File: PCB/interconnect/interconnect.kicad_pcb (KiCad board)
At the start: 2 copper layers, 85 x 56.9 mm, 31 parts, among them J201 XT60-M, J202 5.08mm Screw Terminal, J203 Conn_01x03, J204 Conn_01x03, J205 Conn_01x03, J206 Conn_01x04, J301 Conn_01x15, J302 Conn_01x15, J501 Conn_01x04, J601 Conn_01x04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

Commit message: PCB Rev 1
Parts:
- moved C203 75.0 mm to (136.3, 83.1), turned to 0 degrees
- moved J205 67.8 mm to (132.6, 86.2), turned to 90 degrees
- moved C302 6.22 mm to (109.7, 123.4)
- moved C202 5.08 mm to (63.0, 91.9)
- moved J204 5.08 mm to (67.2, 95.1)
- moved D201 4.08 mm to (127.5, 119.2)
- moved R401 3.95 mm to (68.8, 112.9)
- moved Q401 3.86 mm to (65.6, 110.6)
- moved C201 3.86 mm to (65.6, 113.8)
- moved J203 2.54 mm to (67.2, 116.7)
- moved J201 1.65 mm to (132.0, 108.5)
- moved J202 1.54 mm to (134.8, 123.7)
- moved J701 1.27 mm to (74.2, 116.7)
- moved C701 1.27 mm to (75.5, 119.9)
- moved J206 1.13 mm to (119.9, 104.0)
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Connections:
- J301 pad 10: /MCUs/ESP32_D27 -> /Connectors/MOTORS.Steering
- J301 pad 11: /MCUs/ESP32_D14 -> /Connectors/MOTORS.ESC
- J301 pad 12: /Connectors/ULTRASONICS.US1_TRIGG -> /Connectors/ULTRASONICS.US1_ECHO
- J301 pad 13: /Connectors/ULTRASONICS.US1_ECHO -> /Connectors/ULTRASONICS.US1_TRIGG
- J301 pad 6: /Connectors/ULTRASONICS.US3_TRIGG -> /Connectors/ULTRASONICS.US3_ECHO
- J301 pad 7: /Connectors/ULTRASONICS.US3_ECHO -> /Connectors/ULTRASONICS.US3_TRIGG
- J301 pad 8: /Connectors/ULTRASONICS.US2_TRIGG -> /Connectors/ULTRASONICS.US2_ECHO
- J301 pad 9: /Connectors/ULTRASONICS.US2_ECHO -> /Connectors/ULTRASONICS.US2_TRIGG
- J302 pad 1: /MCUs/ESP32_D23 -> /Connectors/MOTORS.Magnet
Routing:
- net +5V: track 0.00 -> 158.4 mm, vias 0 -> 4
- net +3V3: track 0.00 -> 40.4 mm
- net /Connectors/MOTORS.Steering: track 0.00 -> 33.1 mm
- net /Connectors/MOTORS.Magnet: track 0.00 -> 24.9 mm
- net /Connectors/MOTORS.ESC: track 0.00 -> 21.9 mm
- net /Connectors/ULTRASONICS.US3_TRIGG: track 0.00 -> 15.0 mm
- net /Connectors/XIAO.SCL: track 0.00 -> 14.5 mm
- net /Connectors/ULTRASONICS.US2_TRIGG: track 0.00 -> 12.4 mm
- net /Connectors/ULTRASONICS.US1_TRIGG: track 0.00 -> 11.8 mm
- net /Connectors/ULTRASONICS.US3_ECHO: track 0.00 -> 11.6 mm
- net /Connectors/XIAO.SDA: track 0.00 -> 10.9 mm
- net /Connectors/ULTRASONICS.US1_ECHO: track 0.00 -> 10.6 mm
- net /Connectors/ULTRASONICS.US2_ECHO: track 0.00 -> 9.31 mm
- net /MCUs/ESP32_D15: track 0.00 -> 7.28 mm
- net Net-(Q401-G): track 0.00 -> 2.40 mm
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- added copper zone on F.Cu, net +3V3
- added copper zone on F.Cu, net +5V
- added copper zone on F.Cu, net /Connectors/ESC_5V
- added copper zone on F.Cu, net /Connectors/Magnet_+
- added copper zone on F.Cu, net /Connectors/Motor_Batt_+
- added copper zone on B.Cu, net GND
- added copper zone on F.Cu, net GND
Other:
- board text added: "C"
- board text added: "CAM"
- board text added: "D"

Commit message: Order
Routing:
- net GND: vias 58 -> 60
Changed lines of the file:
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@@
 		(sheetname "Ultrasonic3")
 		(sheetfile "Ultrasonic.kicad_sch")
-		(attr through_hole)
+		(attr through_hole dnp)
 		(fp_line
 			(start -1.33 -1.33)
@@
 		)
 		(fp_text user "${REFERENCE}"
-			(at 0 3.81 360)
+			(at 0 3.81 0)
 			(layer "F.Fab")
 			(effects
@@
 		(sheetname "Connectors")
 		(sheetfile "connectors.kicad_sch")
-		(attr through_hole)
+		(attr through_hole dnp)
 		(fp_line
 			(start -1.33 6.41)
@@
 		(tags "capacitor")
 		(property "Reference" "C601"
-			(at 0 -1.68 360)
+			(at 0 -1.68 0)
 			(layer "F.SilkS")
 			(hide yes)
@@
 		)
 		(property "Value" "1uF"
-			(at 0 1.68 360)
+			(at 0 1.68 0)
 			(layer "F.Fab")
 			(effects
@@
 		)
 		(fp_text user "${REFERENCE}"
-			(at 0 0 360)
+			(at 0 0 0)
 			(layer "F.Fab")
 			(effects
@@
 		(sheetname "Connectors")
 		(sheetfile "connectors.kicad_sch")
-		(attr through_hole)
+		(attr through_hole dnp)
 		(fp_line
 			(start 1.33 1.27)
@@
 		(sheetname "Connectors")
 		(sheetfile "connectors.kicad_sch")
-		(attr through_hole)
+		(attr through_hole dnp)
 		(fp_line
 			(start -1.33 -1.33)
@@
 		)
 		(fp_text user "${REFERENCE}"
-			(at 0 2.54 360)
+			(at 0 2.54 0)
 			(layer "F.Fab")
 			(effects
@@
 		(sheetname "Connectors")
 		(sheetfile "connectors.kicad_sch")
-		(attr through_hole)
+		(attr through_hole dnp)
 		(fp_line
 			(start 7.68 -5.261)
@@
 		(sheetname "MCUs")
 		(sheetfile "MCUs.kicad_sch")
-		(attr through_hole)
+		(attr through_hole dnp)
 		(fp_line
 			(start -1.33 -1.33)
@@
 		(sheetname "Ultrasonic1")
 		(sheetfile "Ultrasonic.kicad_sch")
-		(attr through_hole)
+		(attr through_hole dnp)
 		(fp_line
 			(start -1.33 -1.33)
@@
 		)
 		(fp_text user "${REFERENCE}"
-			(at 0 3.81 360)
+			(at 0 3.81 0)
 			(layer "F.Fab")
 			(effects
@@
 		(sheetname "Ultrasonic2")
 		(sheetfile "Ultrasonic.kicad_sch")
-		(attr through_hole)
+		(attr through_hole dnp)
 		(fp_line
 			(start -1.33 -1.33)
@@
 		)
 		(fp_text user "${REFERENCE}"
-			(at 0 3.81 360)
+			(at 0 3.81 0)
 			(layer "F.Fab")
 			(effects
@@
 		(tags "capacitor")
 		(property "Reference" "C701"
-			(at 0 -1.68 360)
+			(at 0 -1.68 0)
 			(layer "F.SilkS")
 			(hide yes)
@@
 		)
 		(property "Value" "1uF"
-			(at 0 1.68 360)
+			(at 0 1.68 0)
 			(layer "F.Fab")
 			(effects
@@
 		)
 		(fp_text user "${REFERENCE}"
-			(at 0 0 360)
+			(at 0 0 0)
 			(layer "F.Fab")
 			(effects
@@
 		(tags "capacitor")
 		(property "Reference" "C501"
-			(at 0 -1.68 360)
+			(at 0 -1.68 0)
 			(layer "F.SilkS")
 			(hide yes)
@@
 		)
 		(property "Value" "1uF"
-			(at 0 1.68 360)
+			(at 0 1.68 0)
 			(layer "F.Fab")
 			(effects
@@
 		)
 		(fp_text user "${REFERENCE}"
-			(at 0 0 360)
+			(at 0 0 0)
 			(layer "F.Fab")
 			(effects
@@
 		(sheetname "Connectors")
 		(sheetfile "connectors.kicad_sch")
-		(attr through_hole)
+		(attr through_hole dnp)
 		(fp_line
 			(start -9.5 0)
@@
 		(tags "capacitor")
 		(property "Reference" "C203"
-			(at 0 -1.68 360)
+			(at 0 -1.68 0)
 			(layer "F.SilkS")
 			(hide yes)
@@
 		)
 		(property "Value" "1uF"
-			(at 0 1.68 360)
+			(at 0 1.68 0)
 			(layer "F.Fab")
 			(effects
@@
 		)
 		(fp_text user "${REFERENCE}"
-			(at 0 0 360)
+			(at 0 0 0)
 			(layer "F.Fab")
 			(effects
@@
 		(sheetname "Connectors")
 		(sheetfile "connectors.kicad_sch")
-		(attr through_hole)
+		(attr through_hole dnp)
 		(fp_line
 			(start -1.33 6.41)
@@
 		(sheetname "MCUs")
 		(sheetfile "MCUs.kicad_sch")
-		(attr through_hole)
+		(attr through_hole dnp)
 		(fp_line
 			(start -1.33 -1.33)
@@
 	)
 	(gr_text "P"
-		(at 69.73 119.25 0)
+		(at 69.83 116.79 0)
 		(layer "F.SilkS")
 		(effects
@@
 		)
 	)
+	(gr_text "+"
+		(at 125.73 120.69 0)
+		(layer "F.SilkS")
+		(effects
+			(font
+				(size 1.27 1.27)
+				(thickness 0.1)
+			)
+		)
+	)
+	(gr_text "-"
+		(at 125.73 117.79 0)
+		(layer "F.SilkS")
+		(effects
+			(font
+				(size 1.27 1.27)
+				(thickness 0.1)
+			)
+		)
+	)
 	(segment
 		(start 74.505 117.03)
@@
 	)
 	(via
+		(at 72.93 114.69)
+		(size 0.35)
+		(drill 0.2)
+		(layers "F.Cu" "B.Cu")
+		(free yes)
+		(net 2)
+	)
+	(via
 		(at 89.95 110.89)
 		(size 0.35)
@@
 		(size 0.35)
 		(drill 0.2)
+		(layers "F.Cu" "B.Cu")
+		(free yes)
+		(net 2)
+	)
+	(via
+		(at 75.53 114.59)
+		(size 0.35)
+		(drill 0.2)

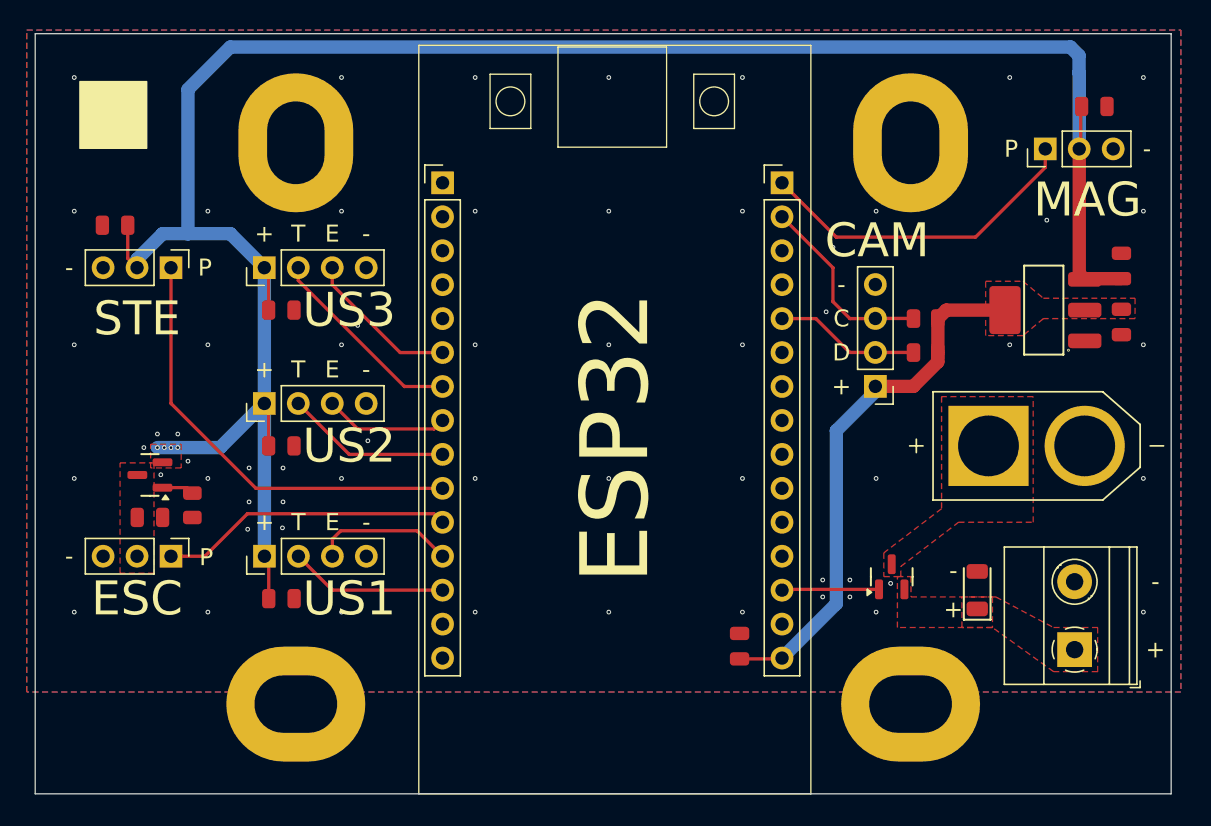
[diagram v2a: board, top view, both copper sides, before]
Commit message: Updated PCB, working inference
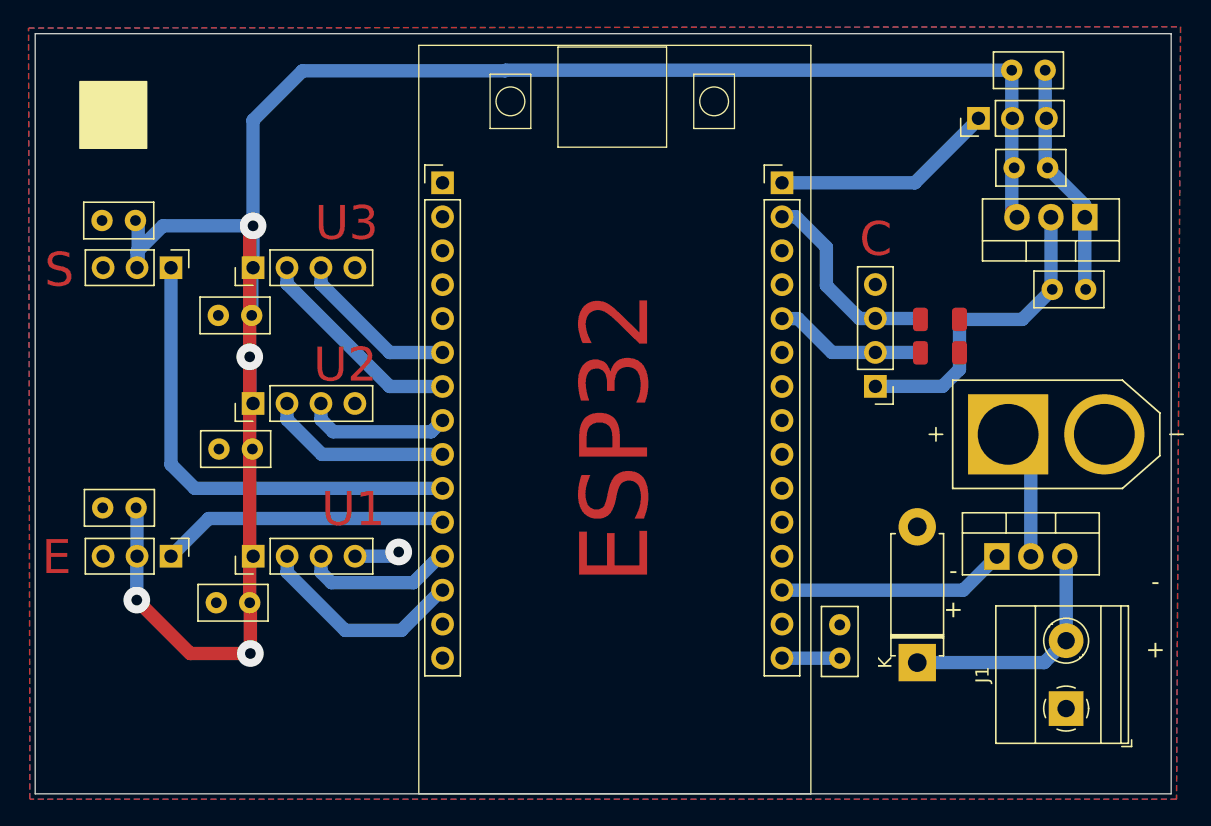
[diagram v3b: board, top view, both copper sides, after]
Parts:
- removed H201, H202, H203, H204: MountingHole_Pad, MountingHole:MountingHole_4.3x6.2mm_M4_Pad
- removed J202: 5.08mm Screw Terminal, TerminalBlock_Phoenix:TerminalBlock_Phoenix_MKDS-1,5-2-5.08_1x02_P5.08mm_Horizontal
- removed Q201: AO3400A, PCM_JLCPCB:Q_SOT-23
- removed Q401: AO3401A, PCM_JLCPCB:Q_SOT-23
- removed R401: 10kΩ, PCM_JLCPCB:R_0805
- removed U401: AMS1117, PCM_JLCPCB:SOT-223-3_L6.5-W3.4-P2.30-LS7.0-BR
- added J1: 5.08mm Screw Terminal, TerminalBlock_Phoenix:TerminalBlock_Phoenix_MKDS-1,5-2-5.08_1x02_P5.08mm_Horizontal, F.Cu at (134.2, 128.1)
- added Q1: IPP060N06N, Package_TO_SOT_THT:TO-220-3_Vertical, F.Cu at (129.0, 116.7)
- added U1: LM317_TO-220, Package_TO_SOT_THT:TO-220-3_Vertical, F.Cu at (135.6, 91.3)
- C201, C202, C203, C302, C401, C402, C501, C601, C701: footprint PCM_JLCPCB:C_0805 -> Capacitor_THT:C_Disc_D5.0mm_W2.5mm_P2.50mm
- D201: footprint PCM_JLCPCB:D_SOD-123FL -> Diode_THT:D_5W_P10.16mm_Horizontal
- R301, R302: footprint PCM_JLCPCB:R_0805 -> PCM_JLCPCB:R_1206
- moved C402 10.9 mm to (130.3, 87.6), turned to 0 degrees
- moved C302 7.55 mm to (117.2, 124.3)
- moved D201 7.04 mm to (123.0, 124.7)
- moved C203 6.75 mm to (130.1, 80.3)
- moved C401 5.73 mm to (133.1, 96.7), turned to 0 degrees
- moved J205 5.50 mm to (127.6, 83.9)
- moved C701 2.39 mm to (73.1, 120.2), turned to 180 degrees
- moved C501 2.25 mm to (73.2, 98.7), turned to 180 degrees
- moved C601 2.18 mm to (73.3, 108.7), turned to 180 degrees
- moved J201 1.71 mm to (133.4, 107.6)
- moved C202 1.57 mm to (64.5, 91.6)
- moved C201 1.26 mm to (64.6, 113.1), turned to 180 degrees
- moved R301 1.07 mm to (124.7, 99.0)
- moved R302 1.07 mm to (124.7, 101.5)
- moved J501 0.84 mm to (73.3, 95.1)
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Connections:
- C201 pad 1: /Connectors/ESC_5V -> +5V
- J203 pad 2: /Connectors/ESC_5V -> +5V
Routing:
- net GND: track 0.00 -> 21.1 mm, vias 60 -> 1
- net /Connectors/Magnet_+: track 0.00 -> 18.2 mm
- net +3V3: track 40.4 -> 28.2 mm
- net /MCUs/ESP32_D15: track 7.28 -> 17.1 mm
- net /Connectors/Motor_Batt_+: track 0.00 -> 9.41 mm
- net /Connectors/MOTORS.Magnet: track 24.9 -> 16.7 mm
- net +5V: track 158.4 -> 151.6 mm
- net /Connectors/ULTRASONICS.US1_TRIGG: track 11.8 -> 15.9 mm
- net /Connectors/MOTORS.Steering: track 33.1 -> 35.8 mm
- net Net-(Q401-G): track 2.40 -> 0.00 mm
- net /Connectors/ULTRASONICS.US2_ECHO: track 9.31 -> 11.0 mm
- net /Connectors/ULTRASONICS.US2_TRIGG: track 12.4 -> 13.9 mm
- net /Connectors/ULTRASONICS.US3_TRIGG: track 15.0 -> 16.0 mm
- net /Connectors/ULTRASONICS.US1_ECHO: track 10.6 -> 11.4 mm
- net /Connectors/ULTRASONICS.US3_ECHO: track 11.6 -> 12.4 mm
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- removed copper zone on F.Cu, net +3V3
- removed copper zone on F.Cu, net +5V
- removed copper zone on F.Cu, net /Connectors/ESC_5V
- removed copper zone on F.Cu, net /Connectors/Magnet_+
- removed copper zone on F.Cu, net /Connectors/Motor_Batt_+
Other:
- board text added: "S"
- board text added: "U1"
- board text added: "U2"
- board text added: "U3"
- board text removed: "CAM"
- board text removed: "D"
- board text removed: "ESC"
- board text removed: "MAG"
- board text removed: "P"
- board text removed: "STE"
- board text removed: "T"
- board text removed: "US1"
- board text removed: "US2"
- board text removed: "US3"
